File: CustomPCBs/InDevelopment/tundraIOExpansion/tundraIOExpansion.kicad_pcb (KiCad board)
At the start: 4 copper layers, 46 x 36.5 mm, 58 parts, among them J1 Conn_01x25, J2 Conn_ARM_SWD_TagConnect_TC203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, J3 Conn_ARM_SWD_TagConnect_TC203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, U1 RP2040, U2 W25Q32JVSS, U4 W25Q32JVSS, U5 RP2040, Y1 12.000MHz, Y2 12.000MHz, Y3 32.768kHz

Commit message: Schematic of new board looks complete for now
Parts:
- removed C15, C16: 22p, Capacitor_SMD:C_0402_1005Metric
- removed J2, J3: Conn_ARM_SWD_TagConnect_TC2030-NL, Connector:Tag-Connect_TC2030-IDC-NL_2x03_P1.27mm_Vertical
- removed Y3: 32.768kHz, Crystal:Crystal_SMD_2012-2Pin_2.0x1.2mm
- added R11: 10k, Resistor_SMD:R_0201_0603Metric, F.Cu at (103.3, 86.5)
- added R12: 10k, Resistor_SMD:R_0201_0603Metric, F.Cu at (103.3, 88.3)
- added R13: 10k, Resistor_SMD:R_0201_0603Metric, F.Cu at (103.3, 90.0)
- added R14: 10k, Resistor_SMD:R_0201_0603Metric, F.Cu at (103.3, 91.8)
- added R15: 10k, Resistor_SMD:R_0201_0603Metric, F.Cu at (103.3, 93.5)
- added R16: 10k, Resistor_SMD:R_0201_0603Metric, F.Cu at (103.3, 95.3)
- added R17: 10k, Resistor_SMD:R_0201_0603Metric, F.Cu at (105.8, 86.5)
- added R18: 10k, Resistor_SMD:R_0201_0603Metric, F.Cu at (105.8, 88.3)
- added R19: 10k, Resistor_SMD:R_0201_0603Metric, F.Cu at (105.8, 90.0)
- added R20: 10k, Resistor_SMD:R_0201_0603Metric, F.Cu at (105.8, 91.8)
- added R21: 10k, Resistor_SMD:R_0201_0603Metric, F.Cu at (105.8, 93.5)
- added R22: 10k, Resistor_SMD:R_0201_0603Metric, F.Cu at (105.8, 95.3)
- added R23: 10k, Resistor_SMD:R_0201_0603Metric, F.Cu at (108.2, 86.5)
- added R24: 10k, Resistor_SMD:R_0201_0603Metric, F.Cu at (108.2, 88.3)
- added R25: 10k, Resistor_SMD:R_0201_0603Metric, F.Cu at (108.2, 90.0)
- added R26: 10k, Resistor_SMD:R_0201_0603Metric, F.Cu at (108.2, 91.8)
- added R27: 10k, Resistor_SMD:R_0201_0603Metric, F.Cu at (184.2, 86.8)
- added R28: 10k, Resistor_SMD:R_0201_0603Metric, F.Cu at (184.2, 88.5)
- added R29: 10k, Resistor_SMD:R_0201_0603Metric, F.Cu at (184.2, 90.3)
- added R30: 10k, Resistor_SMD:R_0201_0603Metric, F.Cu at (184.2, 92.0)
- added R31: 10k, Resistor_SMD:R_0201_0603Metric, F.Cu at (184.2, 93.8)
- added R33: 10k, Resistor_SMD:R_0201_0603Metric, F.Cu at (184.2, 95.5)
- added T1: BSS138BKS_115, footprints:SOT363, F.Cu at (97.3, 61.0)
- added T2: BSS138BKS_115, footprints:SOT363, F.Cu at (97.3, 64.0)
- added T3: BSS138BKS_115, footprints:SOT363, F.Cu at (97.3, 67.0)
- added T4: BSS138BKS_115, footprints:SOT363, F.Cu at (97.3, 70.0)
- added T5: BSS138BKS_115, footprints:SOT363, F.Cu at (97.3, 73.0)
- added T6: BSS138BKS_115, footprints:SOT363, F.Cu at (187.0, 87.4)
- added T7: BSS138BKS_115, footprints:SOT363, F.Cu at (187.0, 90.4)
- added U6: MOUDLE-SEEEDUINO-XIAO-ESP32C3, footprints:MOUDLE14P-SMD-2.54-21X17.8MM, F.Cu at (168.7, 70.5)
- C13, C14: value 100n -> 1u; footprint Capacitor_SMD:C_0402_1005Metric -> Capacitor_SMD:C_0201_0603Metric
- J1: footprint my_connectors:25PIN FRONT FLIP 0.6mm PITCH AYF332535A -> footprints:25PIN FRONT FLIP 0.6mm PITCH AYF332535A
- R3, R4: footprint Resistor_SMD:R_0402_1005Metric -> Resistor_SMD:R_0201_0603Metric
- R5, R6: value 2k2 -> 10k; footprint Resistor_SMD:R_0402_1005Metric -> Resistor_SMD:R_0201_0603Metric
- U3: value ~ -> HE6206-18NR; footprint Package_LGA:LGA-28_5.2x3.8mm_P0.5mm -> Package_TO_SOT_SMD:SOT-23-3
- moved R1 58.1 mm to (98.2, 86.7), turned to 0 degrees
- moved R9 56.9 mm to (98.2, 94.6), turned to 0 degrees
- moved C2 56.2 mm to (100.4, 62.4), turned to 0 degrees
- moved C1 56.0 mm to (100.4, 60.5), turned to 0 degrees
- moved C3 54.3 mm to (100.4, 64.4), turned to 0 degrees
- moved Y1 54.0 mm to (89.0, 93.8), turned to 0 degrees
- moved C6 53.4 mm to (100.4, 70.3), turned to 0 degrees
- moved C7 53.3 mm to (100.4, 72.3), turned to 0 degrees
- moved C10 53.1 mm to (103.3, 64.4), turned to 0 degrees
- moved C9 50.9 mm to (103.3, 62.4), turned to 0 degrees
- moved C8 48.3 mm to (103.3, 60.5), turned to 0 degrees
- moved C4 47.7 mm to (100.4, 66.4), turned to 0 degrees
- moved R2 46.9 mm to (98.2, 88.6), turned to 0 degrees
- moved C5 45.0 mm to (100.4, 68.3), turned to 0 degrees
- moved R8 44.7 mm to (98.2, 92.6), turned to 0 degrees
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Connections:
- C13 pad 2: +3V3 -> +3.3V
- C14 pad 2: Net-(U3-CAP) -> +1V8
- FINGER1 pad 2: Net-(FINGER1-Pin_2) -> SDA1_1V8
- FINGER1 pad 3: Net-(FINGER1-Pin_3) -> SCL1_1V8
- FINGER1 pad 4: +3V3 -> +1V8
- FINGER2 pad 2: Net-(FINGER1-Pin_2) -> SDA2_1V8
- FINGER2 pad 3: Net-(FINGER1-Pin_3) -> SCL2_1V8
- FINGER2 pad 4: +3V3 -> +1V8
- FINGER3 pad 2: Net-(FINGER3-Pin_2) -> SDA3_1V8
- FINGER3 pad 3: Net-(FINGER3-Pin_3) -> SCL3_1V8
- FINGER3 pad 4: +3V3 -> +1V8
- FINGER4 pad 2: Net-(FINGER3-Pin_2) -> SDA4_1V8
- FINGER4 pad 3: Net-(FINGER3-Pin_3) -> SCL4_1V8
- FINGER4 pad 4: +3V3 -> +1V8
- FINGER5L1 pad 2: Net-(FINGER5L1-Pin_2) -> SDA5_1V8
- FINGER5L1 pad 3: Net-(FINGER5L1-Pin_3) -> SCL5_1V8
- FINGER5L1 pad 4: +3V3 -> +1V8
- FINGER5R1 pad 2: Net-(FINGER5L1-Pin_2) -> SDA5_1V8
- FINGER5R1 pad 3: Net-(FINGER5L1-Pin_3) -> SCL5_1V8
- FINGER5R1 pad 4: +3V3 -> +1V8
- R3 pad 1: Net-(U3-BOOTN) -> +3.3V
- R3 pad 2: +3V3 -> SCL1_3V3
- R4 pad 1: +3V3 -> +3.3V
- R4 pad 2: Net-(U3-NRST) -> SDA1_3V3
- R5 pad 1: +3V3 -> +3.3V
- R5 pad 2: Net-(FINGER5L1-Pin_3) -> SCL2_3V3
- R6 pad 1: +3V3 -> +3.3V
- R6 pad 2: Net-(FINGER5L1-Pin_2) -> SDA2_3V3
- U1 pad 15: D11-MI_MOSI -> unconnected-(U1-GPIO12-Pad15)
- U1 pad 16: D10-MI_CS -> unconnected-(U1-GPIO13-Pad16)
- U1 pad 17: D13-MI_SCLK -> unconnected-(U1-GPIO14-Pad17)
- U1 pad 18: D12-MI_MISO -> unconnected-(U1-GPIO15-Pad18)
- U1 pad 2: Net-(FINGER1-Pin_3) -> SDA1_3V3
- U1 pad 24: Net-(J2-SWCLK) -> unconnected-(U1-SWCLK-Pad24)
- U1 pad 25: Net-(J2-SWDIO) -> unconnected-(U1-SWD-Pad25)
- U1 pad 26: Net-(J2-~{RESET}) -> unconnected-(U1-RUN-Pad26)
- U1 pad 3: Net-(FINGER1-Pin_2) -> SCL1_3V3
- U1 pad 4: Net-(FINGER3-Pin_3) -> SDA2_3V3
- U1 pad 5: Net-(FINGER3-Pin_2) -> SCL2_3V3
- U3 pad 1: unconnected-(U3-PIN1/DNC-Pad1) -> GND
- U3 pad 2: GND -> +1V8
- U3 pad 3: +3V3 -> +3.3V
- U5 pad 15: unconnected-(U5-GPIO12-Pad15) -> INTER_RP2040_ESP32_UART_TX0
- U5 pad 16: unconnected-(U5-GPIO13-Pad16) -> INTER_RP2040_ESP32_UART_RX0
- U5 pad 2: Net-(FINGER5L1-Pin_3) -> SDA3_3V3
- U5 pad 24: Net-(J3-SWCLK) -> unconnected-(U5-SWCLK-Pad24)
- U5 pad 25: Net-(J3-SWDIO) -> unconnected-(U5-SWD-Pad25)
- U5 pad 26: Net-(J3-~{RESET}) -> unconnected-(U5-RUN-Pad26)
- U5 pad 3: Net-(FINGER5L1-Pin_2) -> SCL3_3V3
- U5 pad 4: unconnected-(U5-GPIO2-Pad4) -> SDA4_3V3
- U5 pad 5: unconnected-(U5-GPIO3-Pad5) -> SCL4_3V3
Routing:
- net Net-(FINGER5L1-Pin_2): track 65.5 -> 0.00 mm, vias 2 -> 0
- net Net-(FINGER5L1-Pin_3): track 62.6 -> 0.00 mm, vias 4 -> 0
- net GND: track 60.6 -> 0.00 mm, vias 34 -> 0
- net +3V3: track 53.5 -> 0.00 mm, vias 29 -> 0
- net INTER_RP2040_UART_TX1: track 51.5 -> 0.00 mm, vias 2 -> 0
- net INTER_RP2040_UART_RX1: track 49.2 -> 0.00 mm, vias 2 -> 0
- net Net-(FingerAux1-Pin_3): track 40.6 -> 0.00 mm, vias 2 -> 0
- net Net-(FingerAux1-Pin_2): track 39.4 -> 0.00 mm, vias 2 -> 0
- net Net-(FingerAux1-Pin_1): track 38.4 -> 0.00 mm, vias 2 -> 0
- net Net-(FingerAux1-Pin_4): track 32.5 -> 0.00 mm, vias 2 -> 0
- net Net-(FingerAux1-Pin_5): track 32.1 -> 0.00 mm, vias 2 -> 0
- net Net-(FingerAux1-Pin_6): track 28.8 -> 0.00 mm, vias 2 -> 0
- net Net-(FingerAux1-Pin_7): track 27.2 -> 0.00 mm, vias 2 -> 0
- net Net-(FINGER1-Pin_3): track 27.1 -> 0.00 mm, vias 2 -> 0
- net Net-(USB2-Pin_1): track 27.1 -> 0.00 mm, vias 2 -> 0
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
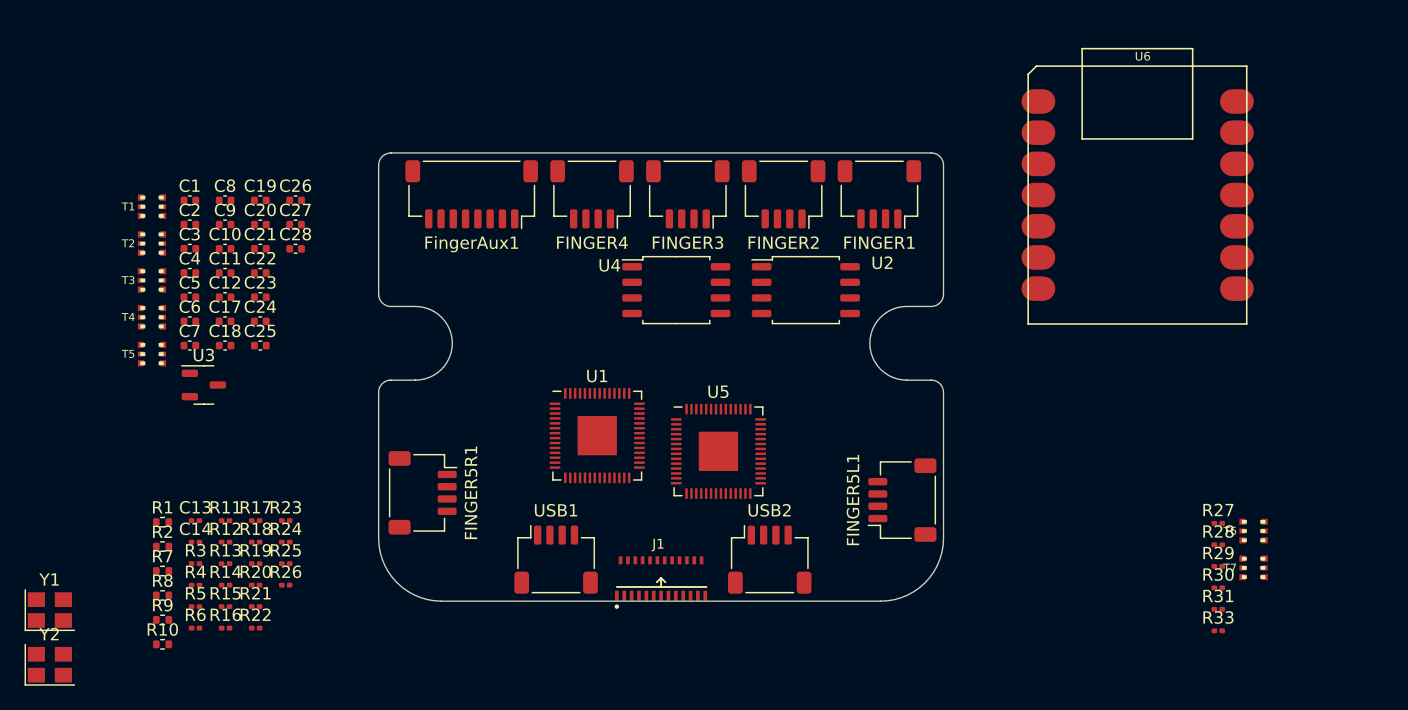
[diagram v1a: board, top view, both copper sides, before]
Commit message: Adding JLCPCB refs and choosing JLCPCB crystals
Adjusting cap values too, since the load capacitance also changes a bit
on the crystal I chose.
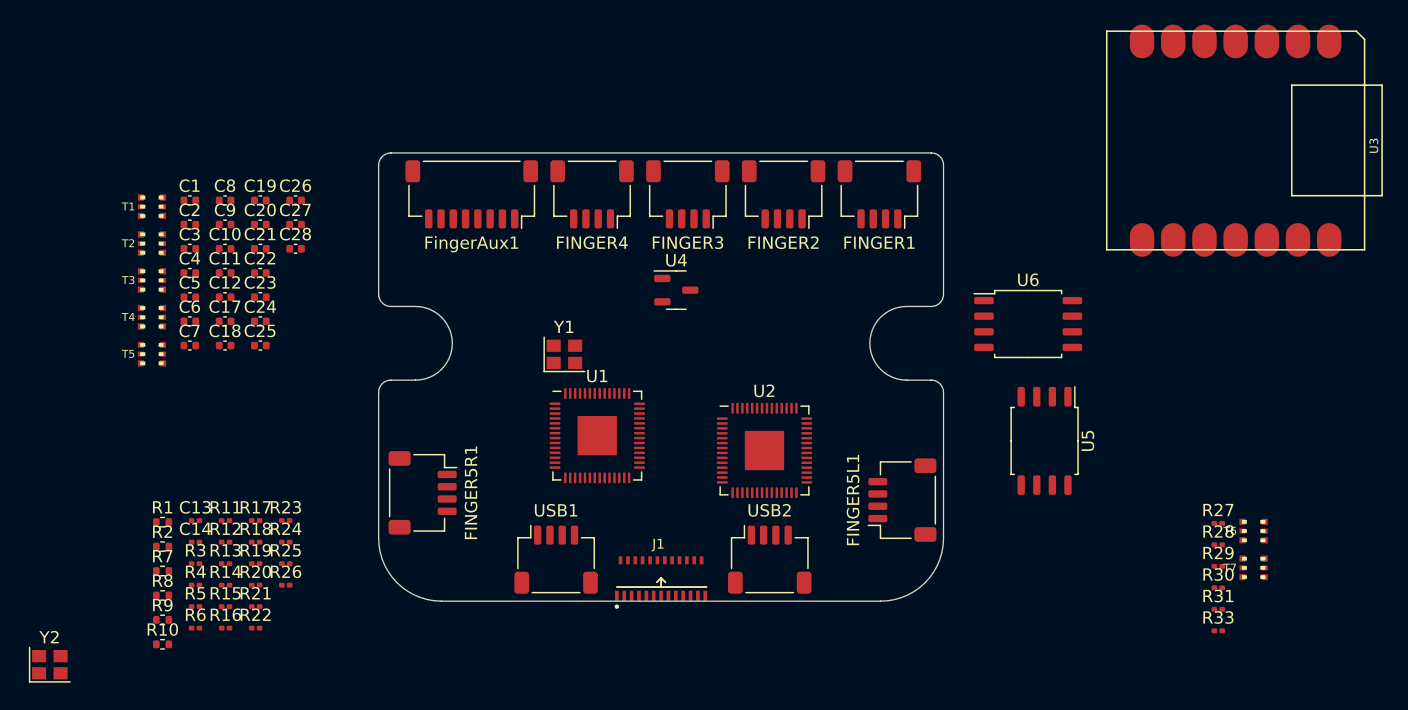
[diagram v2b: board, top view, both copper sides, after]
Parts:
- C11, C12, C19, C21: value 27p -> 33p
- U2: value W25Q32JVSS -> RP2040; footprint Package_SO:SOIC-8_5.23x5.23mm_P1.27mm -> Package_DFN_QFN:QFN-56-1EP_7x7mm_P0.4mm_EP3.2x3.2mm
- U3: value HE6206-18NR -> MOUDLE-SEEEDUINO-XIAO-ESP32C3; footprint Package_TO_SOT_SMD:SOT-23-3 -> footprints:MOUDLE14P-SMD-2.54-21X17.8MM
- U4: value W25Q32JVSS -> HE6206-18NR; footprint Package_SO:SOIC-8_5.23x5.23mm_P1.27mm -> Package_TO_SOT_SMD:SOT-23-3
- U5: value RP2040 -> W25Q32JVSS; footprint Package_DFN_QFN:QFN-56-1EP_7x7mm_P0.4mm_EP3.2x3.2mm -> Package_SO:SOIC-8_5.23x5.23mm_P1.27mm
- U6: value MOUDLE-SEEEDUINO-XIAO-ESP32C3 -> W25Q32JVSS; footprint footprints:MOUDLE14P-SMD-2.54-21X17.8MM -> Package_SO:SOIC-8_5.23x5.23mm_P1.27mm
- Y1, Y2: footprint Crystal:Crystal_SMD_3225-4Pin_3.2x2.5mm -> Crystal:Crystal_SMD_2520-4Pin_2.5x2.0mm
- moved U3 79.0 mm to (175.1, 46.7), turned to -90 degrees
- moved Y1 46.8 mm to (130.9, 73.0)
- moved U5 26.6 mm to (170.0, 80.0), turned to -90 degrees
- moved U2 13.5 mm to (147.2, 80.8)
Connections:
- C19 pad 1: Net-(U5-XIN) -> Net-(U2-XIN)
- C23 pad 1: Net-(U5-VREG_VOUT) -> Net-(U2-VREG_VOUT)
- C25 pad 1: Net-(U5-VREG_VOUT) -> Net-(U2-VREG_VOUT)
- C27 pad 1: Net-(U5-VREG_VOUT) -> Net-(U2-VREG_VOUT)
- C28 pad 1: Net-(U5-ADC_AVDD) -> Net-(U2-ADC_AVDD)
- R10 pad 1: Net-(U4-~{CS}) -> Net-(U2-QSPI_SS)
- R7 pad 2: Net-(U5-XOUT) -> Net-(U2-XOUT)
- R8 pad 2: Net-(U5-ADC_AVDD) -> Net-(U2-ADC_AVDD)
- U2 pad 1: Net-(U1-QSPI_SS) -> +3V3
- U2 pad 2: Net-(U1-QSPI_SD1) -> SDA3_3V3
- U2 pad 3: Net-(U1-QSPI_SD2) -> SCL3_3V3
- U2 pad 4: GND -> SDA4_3V3
- U2 pad 5: Net-(U1-QSPI_SD0) -> SCL4_3V3
- U2 pad 6: Net-(U1-QSPI_SCLK) -> INTER_RP2040_UART_RX1
- U2 pad 7: Net-(U1-QSPI_SD3) -> INTER_RP2040_UART_TX1
- U2 pad 8: +3V3 -> unconnected-(U2-GPIO6-Pad8)
- U3 pad 1: GND -> unconnected-(U3-PA02_A0_D0-Pad1)
- U3 pad 2: +1V8 -> unconnected-(U3-PA4_A1_D1-Pad2)
- U3 pad 3: +3.3V -> unconnected-(U3-PA10_A2_D2-Pad3)
- U4 pad 1: Net-(U4-~{CS}) -> GND
- U4 pad 2: Net-(U4-DO(IO1)) -> +1V8
- U4 pad 3: Net-(U4-IO2) -> +3.3V
- U5 pad 1: +3V3 -> Net-(U1-QSPI_SS)
- U5 pad 2: SDA3_3V3 -> Net-(U1-QSPI_SD1)
- U5 pad 3: SCL3_3V3 -> Net-(U1-QSPI_SD2)
- U5 pad 4: SDA4_3V3 -> GND
- U5 pad 5: SCL4_3V3 -> Net-(U1-QSPI_SD0)
- U5 pad 6: INTER_RP2040_UART_RX1 -> Net-(U1-QSPI_SCLK)
- U5 pad 7: INTER_RP2040_UART_TX1 -> Net-(U1-QSPI_SD3)
- U5 pad 8: unconnected-(U5-GPIO6-Pad8) -> +3V3
- U6 pad 1: unconnected-(U6-PA02_A0_D0-Pad1) -> Net-(U2-QSPI_SS)
- U6 pad 2: unconnected-(U6-PA4_A1_D1-Pad2) -> Net-(U2-QSPI_SD1)
- U6 pad 3: unconnected-(U6-PA10_A2_D2-Pad3) -> Net-(U2-QSPI_SD2)
- U6 pad 4: unconnected-(U6-PA11_A3_D3-Pad4) -> GND
- U6 pad 5: SDA5_3V3 -> Net-(U2-QSPI_SD0)
- U6 pad 6: SCL5_3V3 -> Net-(U2-QSPI_SCLK)
- U6 pad 7: INTER_RP2040_ESP32_UART_RX0 -> Net-(U2-QSPI_SD3)
- U6 pad 8: INTER_RP2040_ESP32_UART_TX0 -> +3V3
- USB2 pad 2: Net-(U5-USB_DP) -> Net-(U2-USB_DP)
- USB2 pad 3: Net-(U5-USB_DM) -> Net-(U2-USB_DM)
- Y2 pad 1: Net-(U5-XIN) -> Net-(U2-XIN)

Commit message: New XIAO ESP32C3 TH footprint, ICM on main board
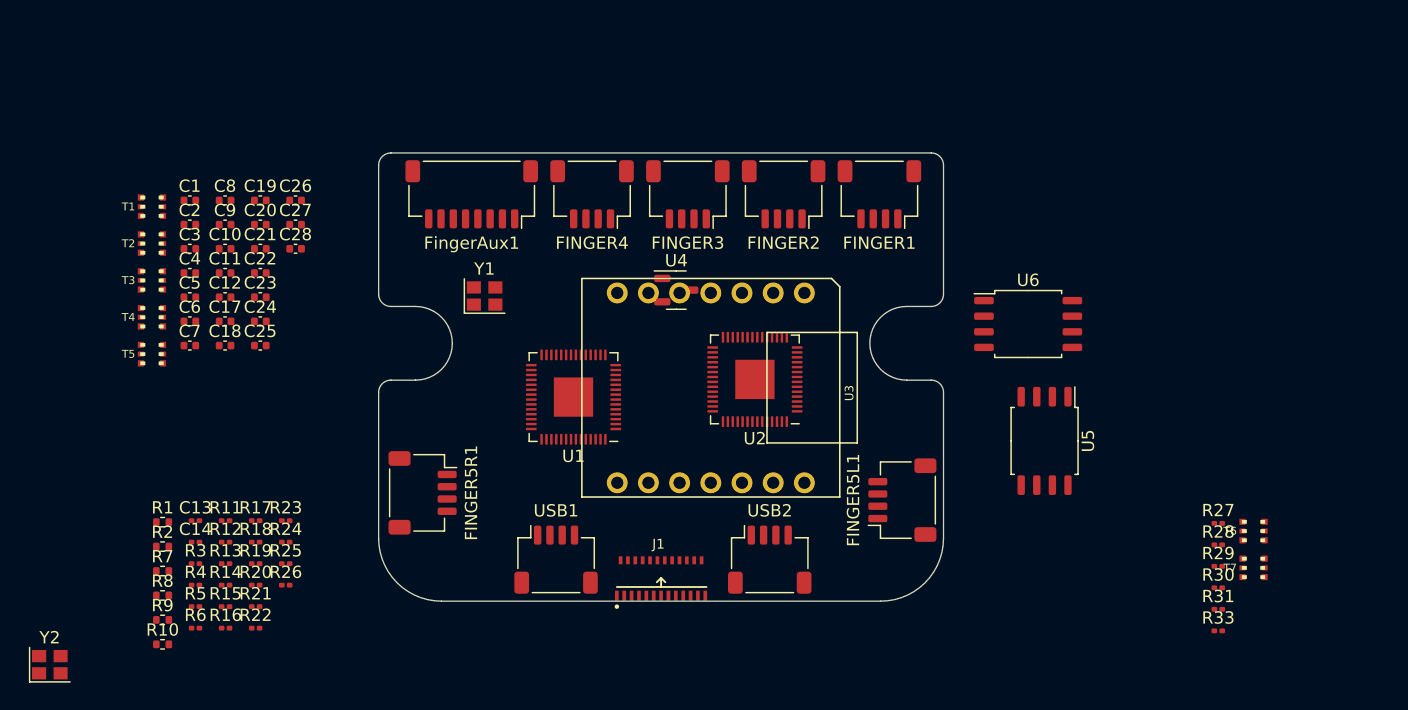
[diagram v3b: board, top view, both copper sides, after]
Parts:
- U3: footprint footprints:MOUDLE14P-SMD-2.54-21X17.8MM -> footprints:MOUDLE14P-SMD-2.54-21X17.8MM_TH
- moved U3 47.2 mm to (132.3, 66.8)
- moved Y1 8.05 mm to (124.4, 68.2)
- moved U2 5.84 mm to (146.4, 75.0), turned to 180 degrees
- moved U1 3.69 mm to (131.6, 76.5), turned to 180 degrees

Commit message: Part positions more or less finished on main board
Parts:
- added C15: 100n, Capacitor_SMD:C_0201_0603Metric, F.Cu at (117.6, 68.0)
- added C16: 100n, Capacitor_SMD:C_0201_0603Metric, F.Cu at (120.3, 68.4)
- added C29: 100n, Capacitor_SMD:C_0201_0603Metric, F.Cu at (119.3, 68.0)
- added R32: 10k, Resistor_SMD:R_0201_0603Metric, F.Cu at (122.8, 66.3)
- added R34: 10k, Resistor_SMD:R_0201_0603Metric, F.Cu at (126.3, 66.3)
- added U7: ICM-20948, Sensor_Motion:InvenSense_QFN-24_3x3mm_P0.4mm, F.Cu at (118.6, 65.7)
- moved R33 68.6 mm to (122.8, 64.9), turned to 90 degrees
- moved T7 67.2 mm to (124.6, 65.6)
- moved R29 65.2 mm to (122.8, 68.1), turned to 90 degrees
- moved T6 65.2 mm to (124.6, 68.8)
- moved R31 64.6 mm to (126.3, 64.9), turned to -90 degrees
- moved R28 64.2 mm to (122.8, 69.5), turned to 90 degrees
- moved R3 63.0 mm to (158.4, 64.5), turned to -90 degrees
- moved R30 62.0 mm to (126.3, 69.5), turned to -90 degrees
- moved R27 60.8 mm to (126.3, 68.1), turned to -90 degrees
- moved R4 59.9 mm to (154.9, 65.9), turned to 90 degrees
- moved R8 59.6 mm to (155.1, 75.1), turned to -135 degrees
- moved T1 59.5 mm to (156.7, 65.2)
- moved R12 59.5 mm to (158.4, 65.9), turned to -90 degrees
- moved R5 57.6 mm to (150.6, 64.5), turned to -90 degrees
- moved R11 56.1 mm to (154.9, 64.5), turned to 90 degrees
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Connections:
- net SDI_1V8 renamed MISO_1V8
- net SDI_3V3 renamed MISO_3V3
- net SDO_1V8 renamed MOSI_1V8
- net SDO_3V3 renamed MOSI_3V3
- T7 pad 3: (no net) -> nCS_3V3
- T7 pad 4: (no net) -> nCS_1V8
- T7 pad 5: (no net) -> +1V8
- U3 pad 4: unconnected-(U3-PA11_A3_D3-Pad4) -> nCS_3V3
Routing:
- net +3V3: track 0.00 -> 24.8 mm, vias 0 -> 10
- net GND: track 0.00 -> 24.0 mm, vias 0 -> 17
- net Net-(U1-VREG_VOUT): track 0.00 -> 5.71 mm
- net Net-(U2-VREG_VOUT): track 0.00 -> 5.68 mm
- net Net-(U2-XIN): track 0.00 -> 4.40 mm
- net Net-(U1-XIN): track 0.00 -> 4.36 mm
- net Net-(U2-ADC_AVDD): track 0.00 -> 2.74 mm
- net Net-(C21-Pad1): track 0.00 -> 2.61 mm
- net Net-(C12-Pad1): track 0.00 -> 2.61 mm
- net +1V8: track 0.00 -> 2.46 mm, vias 0 -> 1
- net Net-(U1-ADC_AVDD): track 0.00 -> 1.81 mm
- net Net-(U2-XOUT): track 0.00 -> 1.72 mm
- net Net-(U1-XOUT): track 0.00 -> 1.71 mm
- net Net-(U7-REGOUT): track 0.00 -> 0.95 mm
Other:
- outline, holes or cut-outs redrawn
